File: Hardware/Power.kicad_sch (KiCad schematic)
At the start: 20 parts, among them IC1 LM74502HDDFR, J1 CarLVPowerConnector, J3 Conn_01x02, Q4 NVMFWS1D7N04XMT1G, Q5 NVMFWS1D7N04XMT1G

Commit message: review council
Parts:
- 24V_TP1, LVGND_TP1: now fitted
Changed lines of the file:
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@@
 		(in_bom no)
 		(on_board yes)
-		(dnp yes)
+		(dnp no)
 		(property "Reference" "LVGND_TP1"
 			(at 37.465 63.119 90)
@@
 		(in_bom no)
 		(on_board yes)
-		(dnp yes)
+		(dnp no)
 		(property "Reference" "24V_TP1"
 			(at 122.174 25.781 0)

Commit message: only 1 crash not bad
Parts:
- removed J3: Conn_01x02, UTSVT_Connectors:Molex_Nano-Fit_105309-xx02_1x02_P2.50mm_Vertical, symbol Connector_Generic:Conn_01x02
- C20: renamed from C5; value 0.1u -> 1u
- R28: renamed from R18; footprint Resistor_SMD:R_0805_2012Metric_Pad1.20x1.40mm_HandSolder -> Resistor_SMD:R_0603_1608Metric_Pad0.98x0.95mm_HandSolder
- renumbered C20 to C14, C19 to C15, C1 to C16, C21 to C17, C3 to C18, C4 to C19, D5 to D11, J1 to J7, Q4 to Q5, Q5 to Q6, R28 to R29, R13 to R30, R1 to R31
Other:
- note removed: "3v3 injector"

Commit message: i hate everything about you - three days grace
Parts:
- 24V_TP1, LVGND_TP1: footprint TestPoint:TestPoint_Pad_2.0x2.0mm -> TestPoint:TestPoint_Keystone_5005-5009_Compact
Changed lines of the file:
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@@
 			)
 		)
-		(property "Footprint" "TestPoint:TestPoint_Pad_2.0x2.0mm"
+		(property "Footprint" "TestPoint:TestPoint_Keystone_5005-5009_Compact"
 			(at 47.625 56.515 0)
 			(effects
@@
 			)
 		)
-		(property "Footprint" "TestPoint:TestPoint_Pad_2.0x2.0mm"
+		(property "Footprint" "TestPoint:TestPoint_Keystone_5005-5009_Compact"
 			(at 128.27 33.655 0)
 			(effects

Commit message: bom, cpl, and friends
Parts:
- D11: Mouser Part Number (none) -> 833-SMAF4758A-TP; P/N (none) -> SMAF4758A-TP

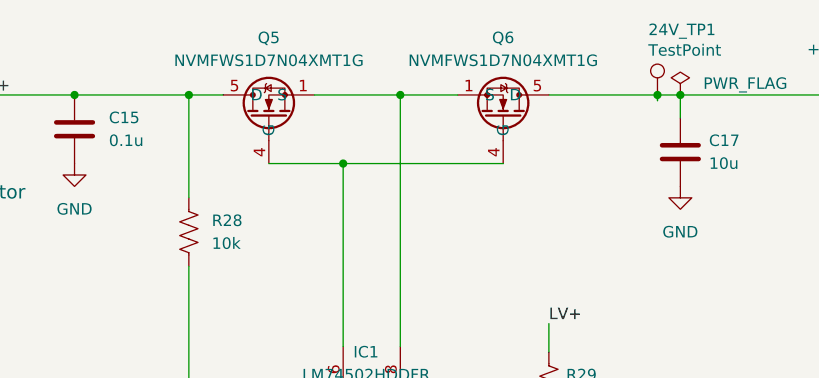
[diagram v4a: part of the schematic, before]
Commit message: updated new smaller NMOS
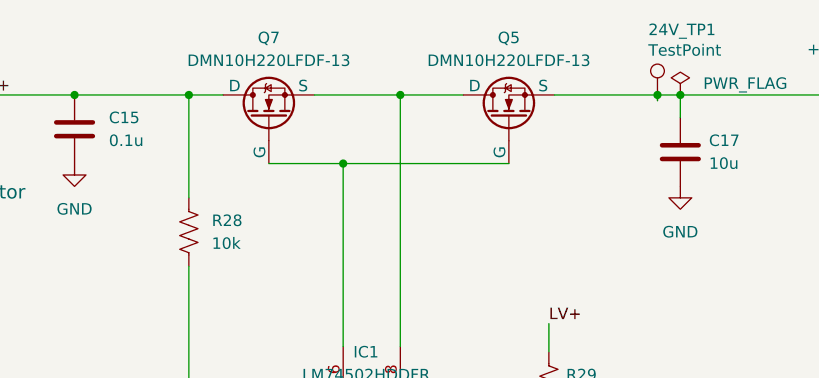
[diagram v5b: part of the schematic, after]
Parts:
- removed Q5, Q6: NVMFWS1D7N04XMT1G, UTSVT_Power:NVMFWS3D0P04M8LT1G, symbol UTSVT_Power:NVMFWS1D7N04XMT1G
- added Q5, Q7: DMN10H220LFDF-13, symbol Simulation_SPICE:NMOS
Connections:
- net +24V: now also Q5.3 (S)
- net LV+: now also Q7.1 (D)
- net at IC1.8 (SRC): now also Q5.1 (D), Q7.3 (S)
- net at IC1.6 (GATE): now also Q5.2 (G), Q7.2 (G)
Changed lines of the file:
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@@
 	)
 	(junction
-		(at 123.19 33.02)
+		(at 59.055 68.58)
 		(diameter 0)
 		(color 0 0 0 0)
 	)
 	(junction
-		(at 59.055 68.58)
+		(at 123.19 33.02)
 		(diameter 0)
 		(color 0 0 0 0)
@@
 	(wire
 		(pts
-			(xy 94.615 33.02) (xy 100.965 33.02)
+			(xy 94.615 33.02) (xy 101.6 33.02)
 		)
 		(stroke
@@
 	(wire
 		(pts
-			(xy 88.265 40.64) (xy 106.045 40.64)
+			(xy 88.265 40.64) (xy 106.68 40.64)
 		)
 		(stroke
@@
 	(wire
 		(pts
-			(xy 111.125 33.02) (xy 123.19 33.02)
+			(xy 107.315 72.39) (xy 111.125 72.39)
 		)
 		(stroke
@@
 	(wire
 		(pts
-			(xy 107.315 72.39) (xy 111.125 72.39)
+			(xy 111.76 33.02) (xy 123.19 33.02)
 		)
 		(stroke
@@
 	)
 	(symbol
-		(lib_id "UTSVT_Power:NVMFWS1D7N04XMT1G")
-		(at 113.03 37.465 270)
-		(mirror x)
-		(unit 1)
-		(exclude_from_sim no)
-		(in_bom no)
-		(on_board yes)
-		(dnp no)
-		(fields_autoplaced yes)
-		(property "Reference" "Q6"
-			(at 106.045 26.67 90)
-			(effects
-				(font
-					(size 1.27 1.27)
-				)
-			)
-		)
-		(property "Value" "NVMFWS1D7N04XMT1G"
-			(at 106.045 29.21 90)
-			(effects
-				(font
-					(size 1.27 1.27)
-				)
-			)
-		)
-		(property "Footprint" "UTSVT_Power:NVMFWS3D0P04M8LT1G"
-			(at 113.03 37.465 0)
-			(effects
-				(font
-					(size 1.27 1.27)
-				)
-				(hide yes)
-			)
-		)
-		(property "Datasheet" "https://www.mouser.com/catalog/specsheets/onsemi_02-27-2025_NVMFWS1D7N04XM-D.pdf"
-			(at 113.03 37.465 0)
-			(effects
-				(font
-					(size 1.27 1.27)
-				)
-				(hide yes)
-			)
-		)
-		(property "Description" "1 N-Channel MOSFETs 40V 154A Id 1.65mOhm Rds 3.5-20V Vgs"
-			(at 113.03 37.465 0)
-			(effects
-				(font
-					(size 1.27 1.27)
-				)
-				(hide yes)
-			)
-		)
-		(property "P/N" "NVMFWS1D7N04XMT1G"
-			(at 113.03 37.465 0)
-			(effects
-				(font
-					(size 1.27 1.27)
-				)
-				(hide yes)
-			)
-		)
-		(property "If" ""
-			(at 113.03 37.465 90)
-			(effects
-				(font
-					(size 1.27 1.27)
-				)
-				(hide yes)
-			)
-		)
-		(property "Vf" ""
-			(at 113.03 37.465 90)
-			(effects
-				(font
-					(size 1.27 1.27)
-				)
-				(hide yes)
-			)
-		)
-		(pin "8"
-		)
-		(pin "5"
-		)
-		(pin "4"
-		)
-		(pin "6"
-		)
-		(pin "7"
-		)
-		(pin "3"
-		)
-		(pin "9"
-		)
-		(pin "1"
-		)
-		(pin "2"
-		)
-		(instances
-			(project "VehicleControlUnit"
-				(path "/795c8e51-3ded-4d21-b864-aaff31c5def7/5469fc22-573e-4402-96df-d8b4b5bb4d29"
-					(reference "Q6")
-					(unit 1)
-				)
-			)
-		)
-	)
-	(symbol
 		(lib_id "power:GND")
 		(at 47.625 62.865 0)
@@
 	)
 	(symbol
-		(lib_id "UTSVT_Power:NVMFWS1D7N04XMT1G")
-		(at 73.025 37.465 90)
+		(lib_id "Simulation_SPICE:NMOS")
+		(at 106.68 35.56 90)
 		(unit 1)
 		(exclude_from_sim no)
-		(in_bom no)
+		(in_bom yes)
 		(on_board yes)
 		(dnp no)
 		(fields_autoplaced yes)
 		(property "Reference" "Q5"
-			(at 80.01 26.67 90)
+			(at 106.68 26.67 90)
 			(effects
 				(font
@@
 			)
 		)
-		(property "Value" "NVMFWS1D7N04XMT1G"
-			(at 80.01 29.21 90)
+		(property "Value" "DMN10H220LFDF-13"
+			(at 106.68 29.21 90)
 			(effects
 				(font
@@
 			)
 		)
-		(property "Footprint" "UTSVT_Power:NVMFWS3D0P04M8LT1G"
-			(at 73.025 37.465 0)
+		(property "Footprint" ""
+			(at 104.14 30.48 0)
 			(effects
 				(font
@@
 			)
 		)
-		(property "Datasheet" "https://www.mouser.com/catalog/specsheets/onsemi_02-27-2025_NVMFWS1D7N04XM-D.pdf"
-			(at 73.025 37.465 0)
+		(property "Datasheet" "https://www.diodes.com/assets/Datasheets/DMN10H220LFDF.pdf"
+			(at 119.38 35.56 0)
 			(effects
 				(font
@@
 			)
 		)
-		(property "Description" "1 N-Channel MOSFETs 40V 154A Id 1.65mOhm Rds 3.5-20V Vgs"
-			(at 73.025 37.465 0)
+		(property "Description" "N-MOSFET transistor, drain/source/gate"
+			(at 106.68 35.56 0)
 			(effects
 				(font
@@
 			)
 		)
-		(property "P/N" "NVMFWS1D7N04XMT1G"
-			(at 73.025 37.465 0)
+		(property "Sim.Device" "NMOS"
+			(at 123.825 35.56 0)
 			(effects
 				(font
@@
 			)
 		)
-		(property "If" ""
-			(at 73.025 37.465 90)
+		(property "Sim.Type" "VDMOS"
+			(at 125.73 35.56 0)
 			(effects
 				(font
@@
 			)
 		)
-		(property "Vf" ""
-			(at 73.025 37.465 90)
+		(property "Sim.Pins" "1=D 2=G 3=S"
+			(at 121.92 35.56 0)
 			(effects
 				(font
@@
 			)
 		)
-		(pin "8"
-		)
-		(pin "5"
-		)
-		(pin "4"
-		)
-		(pin "6"
-		)
-		(pin "7"
-		)
-		(pin "3"
-		)
-		(pin "9"
+		(pin "2"
 		)
 		(pin "1"
 		)
-		(pin "2"
+		(pin "3"
 		)
 		(instances
-			(project ""
+			(project "VehicleControlUnit"
 				(path "/795c8e51-3ded-4d21-b864-aaff31c5def7/5469fc22-573e-4402-96df-d8b4b5bb4d29"
 					(reference "Q5")
@@
 					(unit 1)
 				)
+			)
+		)
+	)
+	(symbol
+		(lib_id "Simulation_SPICE:NMOS")
+		(at 80.01 35.56 90)
+		(unit 1)
+		(exclude_from_sim no)
+		(in_bom yes)
+		(on_board yes)
+		(dnp no)
+		(fields_autoplaced yes)
+		(property "Reference" "Q7"
+			(at 80.01 26.67 90)
+			(effects
+				(font
+					(size 1.27 1.27)
+				)
+			)
+		)
+		(property "Value" "DMN10H220LFDF-13"
+			(at 80.01 29.21 90)
+			(effects
+				(font
+					(size 1.27 1.27)
+				)
+			)
+		)
+		(property "Footprint" ""
+			(at 77.47 30.48 0)
+			(effects
+				(font
+					(size 1.27 1.27)
+				)
+				(hide yes)
+			)
+		)
+		(property "Datasheet" "https://www.diodes.com/assets/Datasheets/DMN10H220LFDF.pdf"
+			(at 92.71 35.56 0)
+			(effects
+				(font
+					(size 1.27 1.27)
+				)
+				(hide yes)
+			)
+		)
+		(property "Description" "N-MOSFET transistor, drain/source/gate"
+			(at 80.01 35.56 0)
+			(effects
+				(font
+					(size 1.27 1.27)
+				)
+				(hide yes)
+			)
+		)
+		(property "Sim.Device" "NMOS"
+			(at 97.155 35.56 0)
+			(effects
+				(font
+					(size 1.27 1.27)
+				)
+				(hide yes)
+			)
+		)
+		(property "Sim.Type" "VDMOS"
+			(at 99.06 35.56 0)
+			(effects
+				(font
+					(size 1.27 1.27)
+				)
+				(hide yes)
+			)
+		)
+		(property "Sim.Pins" "1=D 2=G 3=S"
+			(at 95.25 35.56 0)
+			(effects
+				(font
+					(size 1.27 1.27)
+				)
+				(hide yes)
+			)
+		)
+		(pin "2"
+		)
+		(pin "1"
+		)
+		(pin "3"
+		)
+		(instances
+			(project ""
+				(path "/795c8e51-3ded-4d21-b864-aaff31c5def7/5469fc22-573e-4402-96df-d8b4b5bb4d29"
+					(reference "Q7")
+					(unit 1)
+				)
